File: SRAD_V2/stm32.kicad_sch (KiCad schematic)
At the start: 1 part, among them U11 STM32F767ZIT6

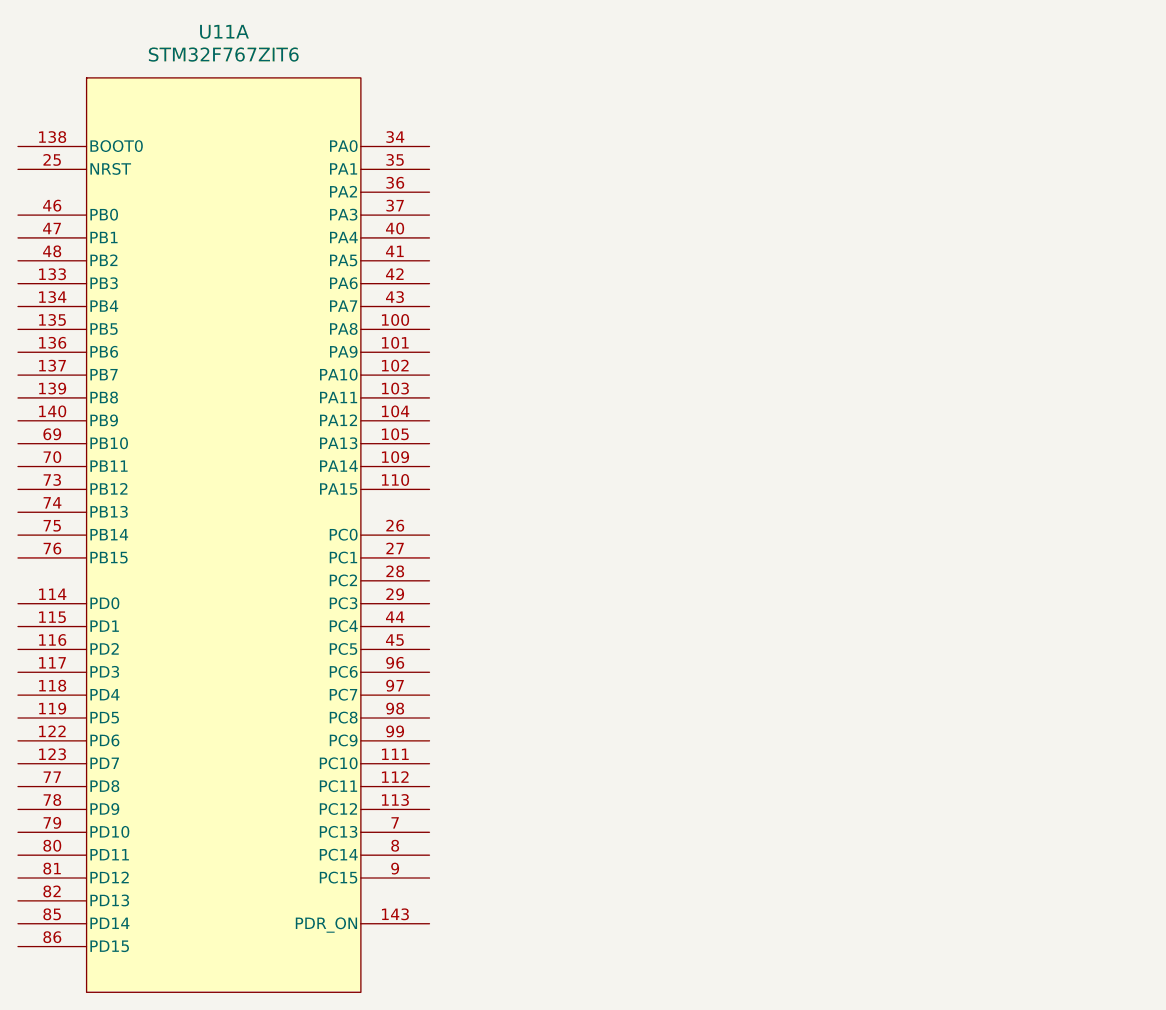
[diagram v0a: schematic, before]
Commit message: created some basic building blocks as hierarchical sheets
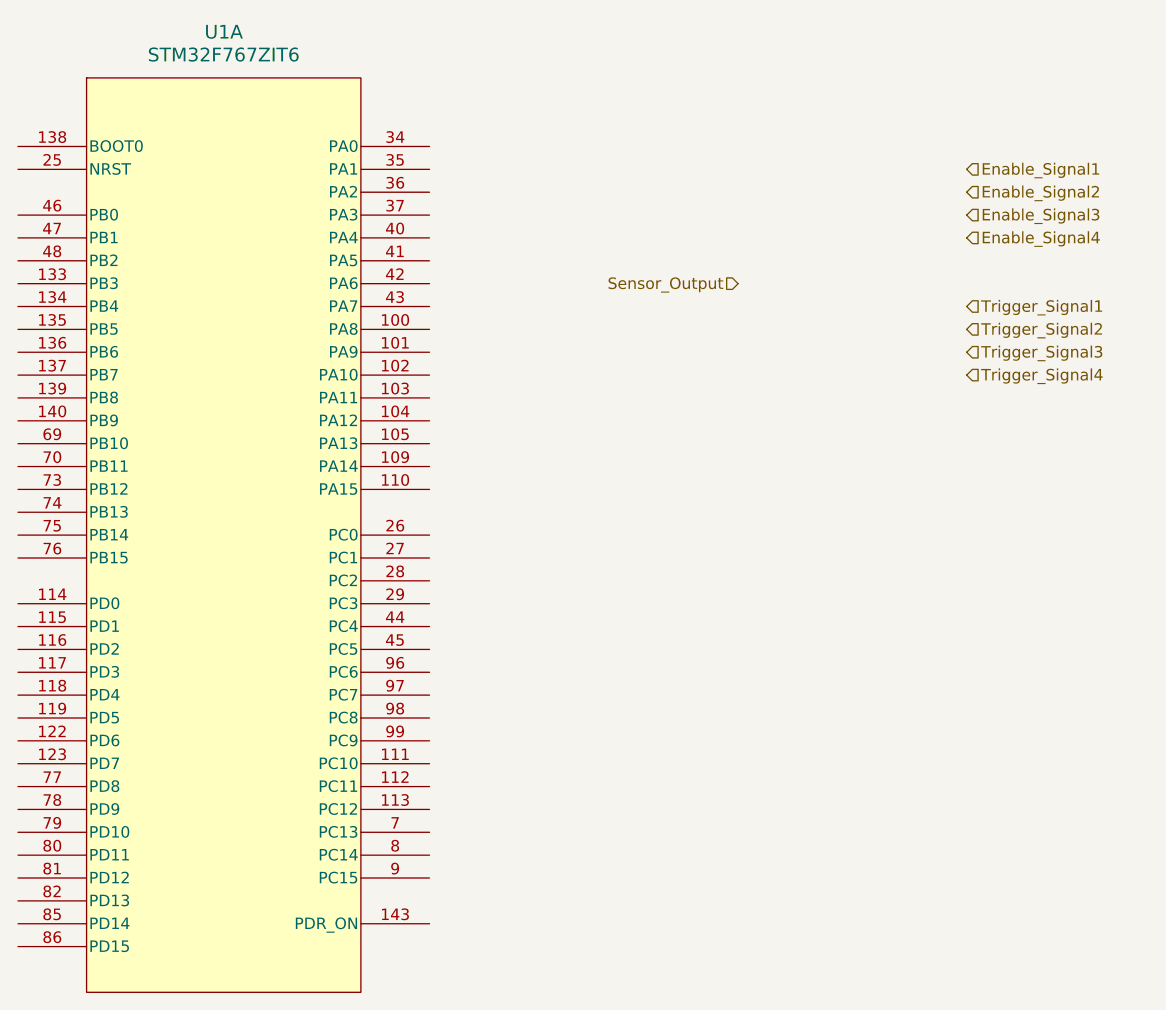
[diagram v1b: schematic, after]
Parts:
- renumbered U11 to U1
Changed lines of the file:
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@@
 	(generator_version "9.0")
 	(paper "A4")
+	(hierarchical_label "Enable_Signal1"
+		(shape input)
+		(at 222.25 58.42 0)
+		(effects
+			(font
+				(size 1.27 1.27)
+			)
+			(justify left)
+		)
+	)
+	(hierarchical_label "Trigger_Signal1"
+		(shape input)
+		(at 222.25 73.66 0)
+		(effects
+			(font
+				(size 1.27 1.27)
+			)
+			(justify left)
+		)
+	)
+	(hierarchical_label "Trigger_Signal4"
+		(shape input)
+		(at 222.25 81.28 0)
+		(effects
+			(font
+				(size 1.27 1.27)
+			)
+			(justify left)
+		)
+	)
+	(hierarchical_label "Sensor_Output"
+		(shape input)
+		(at 196.85 71.12 180)
+		(effects
+			(font
+				(size 1.27 1.27)
+			)
+			(justify right)
+		)
+	)
+	(hierarchical_label "Trigger_Signal3"
+		(shape input)
+		(at 222.25 78.74 0)
+		(effects
+			(font
+				(size 1.27 1.27)
+			)
+			(justify left)
+		)
+	)
+	(hierarchical_label "Trigger_Signal2"
+		(shape input)
+		(at 222.25 76.2 0)
+		(effects
+			(font
+				(size 1.27 1.27)
+			)
+			(justify left)
+		)
+	)
+	(hierarchical_label "Enable_Signal2"
+		(shape input)
+		(at 222.25 60.96 0)
+		(effects
+			(font
+				(size 1.27 1.27)
+			)
+			(justify left)
+		)
+	)
+	(hierarchical_label "Enable_Signal3"
+		(shape input)
+		(at 222.25 63.5 0)
+		(effects
+			(font
+				(size 1.27 1.27)
+			)
+			(justify left)
+		)
+	)
+	(hierarchical_label "Enable_Signal4"
+		(shape input)
+		(at 222.25 66.04 0)
+		(effects
+			(font
+				(size 1.27 1.27)
+			)
+			(justify left)
+		)
+	)
 	(symbol
 		(lib_id "STM32F767ZIT6:STM32F767ZIT6")
@@
 		(dnp no)
 		(fields_autoplaced yes)
-		(property "Reference" "U11"
+		(property "Reference" "U1"
 			(at 139.7 43.18 0)
 			(effects
@@
 			(project "SRAD_V2"
 				(path "/016ea6e5-09c6-43d4-b6cc-3404e2d65458/51825e43-6d17-42cc-86d0-a82f84dc8a84"
-					(reference "U11")
+					(reference "U1")
 					(unit 1)
 				)

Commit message: more changes
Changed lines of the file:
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@@
 	(generator_version "9.0")
 	(paper "A4")
-	(hierarchical_label "Enable_Signal1"
-		(shape input)
-		(at 222.25 58.42 0)
-		(effects
-			(font
-				(size 1.27 1.27)
-			)
-			(justify left)
-		)
-	)
-	(hierarchical_label "Trigger_Signal1"
-		(shape input)
+	(hierarchical_label "CH1"
+		(shape output)
 		(at 222.25 73.66 0)
 		(effects
@@
 		)
 	)
-	(hierarchical_label "Trigger_Signal4"
-		(shape input)
+	(hierarchical_label "CH4"
+		(shape output)
 		(at 222.25 81.28 0)
 		(effects
@@
 		)
 	)
-	(hierarchical_label "Sensor_Output"
+	(hierarchical_label "IVAL"
 		(shape input)
 		(at 196.85 71.12 180)
@@
 		)
 	)
-	(hierarchical_label "Trigger_Signal3"
-		(shape input)
+	(hierarchical_label "CH3"
+		(shape output)
 		(at 222.25 78.74 0)
 		(effects
@@
 		)
 	)
-	(hierarchical_label "Trigger_Signal2"
-		(shape input)
+	(hierarchical_label "CH2"
+		(shape output)
 		(at 222.25 76.2 0)
 		(effects
 			(font
-				(size 1.27 1.27)
-			)
-			(justify left)
-		)
-	)
-	(hierarchical_label "Enable_Signal2"
-		(shape input)
-		(at 222.25 60.96 0)
-		(effects
-			(font
-				(size 1.27 1.27)
-			)
-			(justify left)
-		)
-	)
-	(hierarchical_label "Enable_Signal3"
-		(shape input)
-		(at 222.25 63.5 0)
-		(effects
-			(font
-				(size 1.27 1.27)
-			)
-			(justify left)
-		)
-	)
-	(hierarchical_label "Enable_Signal4"
-		(shape input)
-		(at 222.25 66.04 0)
-		(effects
-			(font
